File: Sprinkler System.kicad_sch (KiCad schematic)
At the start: 76 parts, among them J1 Main Supply, J2 XFMR_Out, J20 Station_0, J21 Station_1, J22 Station_2, J23 Station_3, J24 Station_4, J25 Station_5, J3 XFMR_In, J4 Conn_Button, J5 UART0, J6 I2C, K1 G3MB-202P, K20 G5LE-1-DC5, K21 G5LE-1-DC5, K22 G5LE-1-DC5, K23 G5LE-1-DC5, K24 G5LE-1-DC5, K25 G5LE-1-DC5, SW1 EN, SW2 BOOT, U1 AMS1117-3.3, U2 EL817, U3 HLK-PM01, U4 ESP32-WROOM-32U, U5 ULN2803A

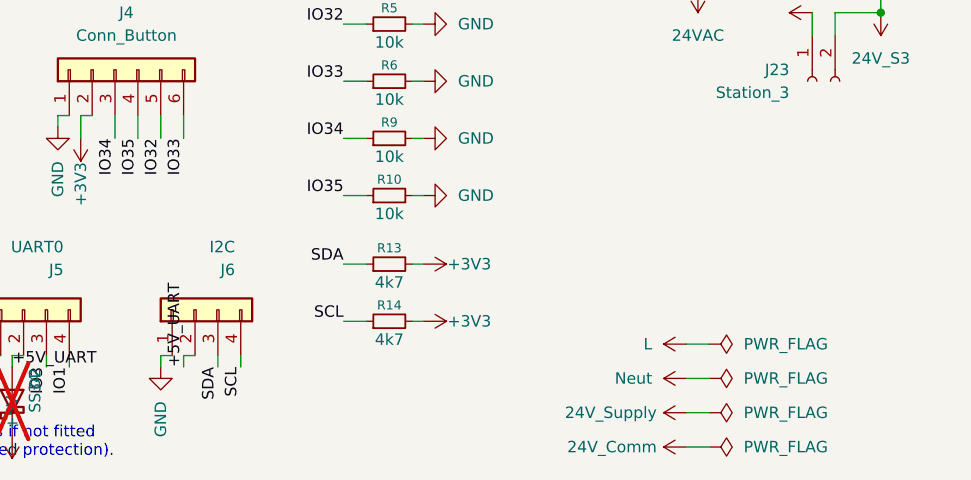
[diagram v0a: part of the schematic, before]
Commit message: Add JP1 solder jumper to select J6 I2C-header supply (3V3 default)
The I2C expansion header J6 previously took the raw +5V_UART branch on
pin 2, which would put 5V on the SDA/SCL pull-ups and any 3V3-logic
peripheral. JP1 (3-way solder jumper on the back) selects J6's VCC:
default-bridged 1-2 = +3V3, re-bridge 2-3 = +5V. J6 pin 2 is now the
/J6_VCC net; J5 pin 2 keeps the true +5V_UART (re-fed from the rail on
F.Cu past the IO-routing on the back), so UART-adapter powering and the
D2 back-feed block are unaffected.

Scope note: the optional TCA9406 level-shifter and SDA/SCL bypass
jumpers from the original plan were dropped - the J5/J6 corner is too
congested to route them cleanly on this revision, and the supply
jumper alone covers the intended use (run a 3V3 I2C device safely, or
switch to 5V if ever needed). Can be revisited interactively later.

Jumper is on B.Cu, silk-labelled. ERC/DRC: 0 violations; zones refilled.

Co-Authored-By: Claude Fable 5 <noreply@anthropic.com>
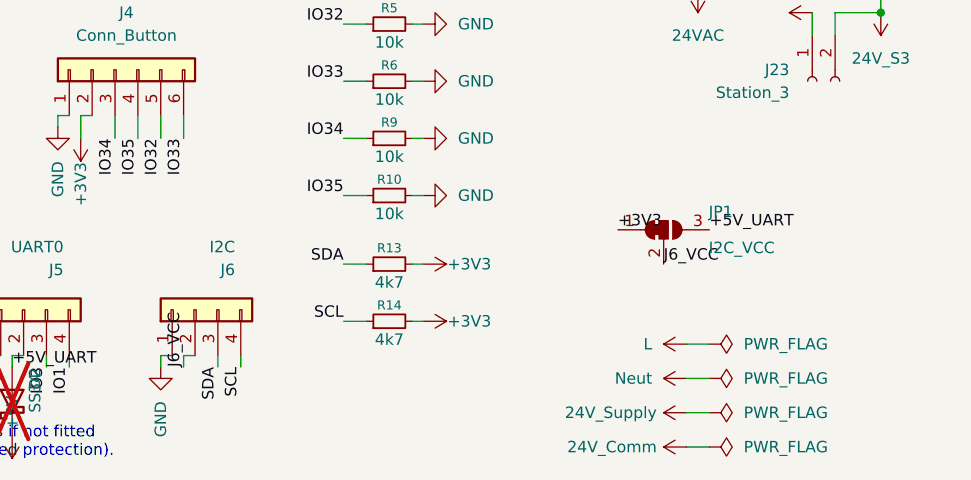
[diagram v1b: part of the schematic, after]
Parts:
- added JP1: I2C_VCC, Jumper:SolderJumper-3_P1.3mm_Bridged12_RoundedPad1.0x1.5mm_NumberLabels, symbol Jumper:SolderJumper_3_Bridged12
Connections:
- net +3V3: now also JP1.1 (A)
- net +5V_UART: now also JP1.3 (B); no longer J6.2 (Pin_2)
- new net J6_VCC: J6.2 (Pin_2), JP1.2 (C)
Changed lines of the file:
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@@
 		)
 	)
-	(label "+5V_UART"
+	(label "J6_VCC"
 		(at 101.6 185.42 90)
 		(effects
@@
 		(effects
 			(font
+				(size 1.27 1.27)
+			)
+			(justify left bottom)
+		)
+	)
+	(symbol
+		(lib_id "Jumper:SolderJumper_3_Bridged12")
+		(at 154.94 170.18 0)
+		(unit 1)
+		(body_style 1)
+		(exclude_from_sim no)
+		(in_bom yes)
+		(on_board yes)
+		(in_pos_files yes)
+		(dnp no)
+		(fields_autoplaced yes)
+		(property "Reference" "JP1"
+			(at 159.94 168.18 0)
+			(show_name no)
+			(do_not_autoplace no)
+			(effects
+				(font
+					(size 1.27 1.27)
+				)
+				(justify left)
+			)
+		)
+		(property "Value" "I2C_VCC"
+			(at 159.94 172.18 0)
+			(show_name no)
+			(do_not_autoplace no)
+			(effects
+				(font
+					(size 1.27 1.27)
+				)
+				(justify left)
+			)
+		)
+		(property "Footprint" "Jumper:SolderJumper-3_P1.3mm_Bridged12_RoundedPad1.0x1.5mm_NumberLabels"
+			(at 154.94 170.18 0)
+			(hide yes)
+			(show_name no)
+			(do_not_autoplace no)
+			(effects
+				(font
+					(size 1.27 1.27)
+				)
+				(justify left)
+			)
+		)
+		(property "Datasheet" ""
+			(at 154.94 170.18 0)
+			(hide yes)
+			(show_name no)
+			(do_not_autoplace no)
+			(effects
+				(font
+					(size 1.27 1.27)
+				)
+				(justify left)
+			)
+		)
+		(property "Description" "J6 supply select: 1-2=3V3 (default bridged), 2-3=5V"
+			(at 154.94 170.18 0)
+			(hide yes)
+			(show_name no)
+			(do_not_autoplace no)
+			(effects
+				(font
+					(size 1.27 1.27)
+				)
+				(justify left)
+			)
+		)
+		(pin "1"
+		)
+		(pin "2"
+		)
+		(pin "3"
+		)
+		(instances
+			(project "Sprinkler System"
+				(path "/8fa12040-b3d8-4f13-b02e-6c4ba5cdd128"
+					(reference "JP1")
+					(unit 1)
+				)
+			)
+		)
+	)
+	(label "+3V3"
+		(at 149.85999999999999 170.18 0)
+		(effects
+			(font
+				(size 1.27 1.27)
+			)
+			(justify left bottom)
+		)
+	)
+	(label "J6_VCC"
+		(at 154.94 173.99 0)
+		(effects
+			(font
+				(size 1.27 1.27)
+			)
+			(justify left bottom)
+		)
+	)
+	(label "+5V_UART"
+		(at 160.02 170.18 0)
+		(effects
+			(font

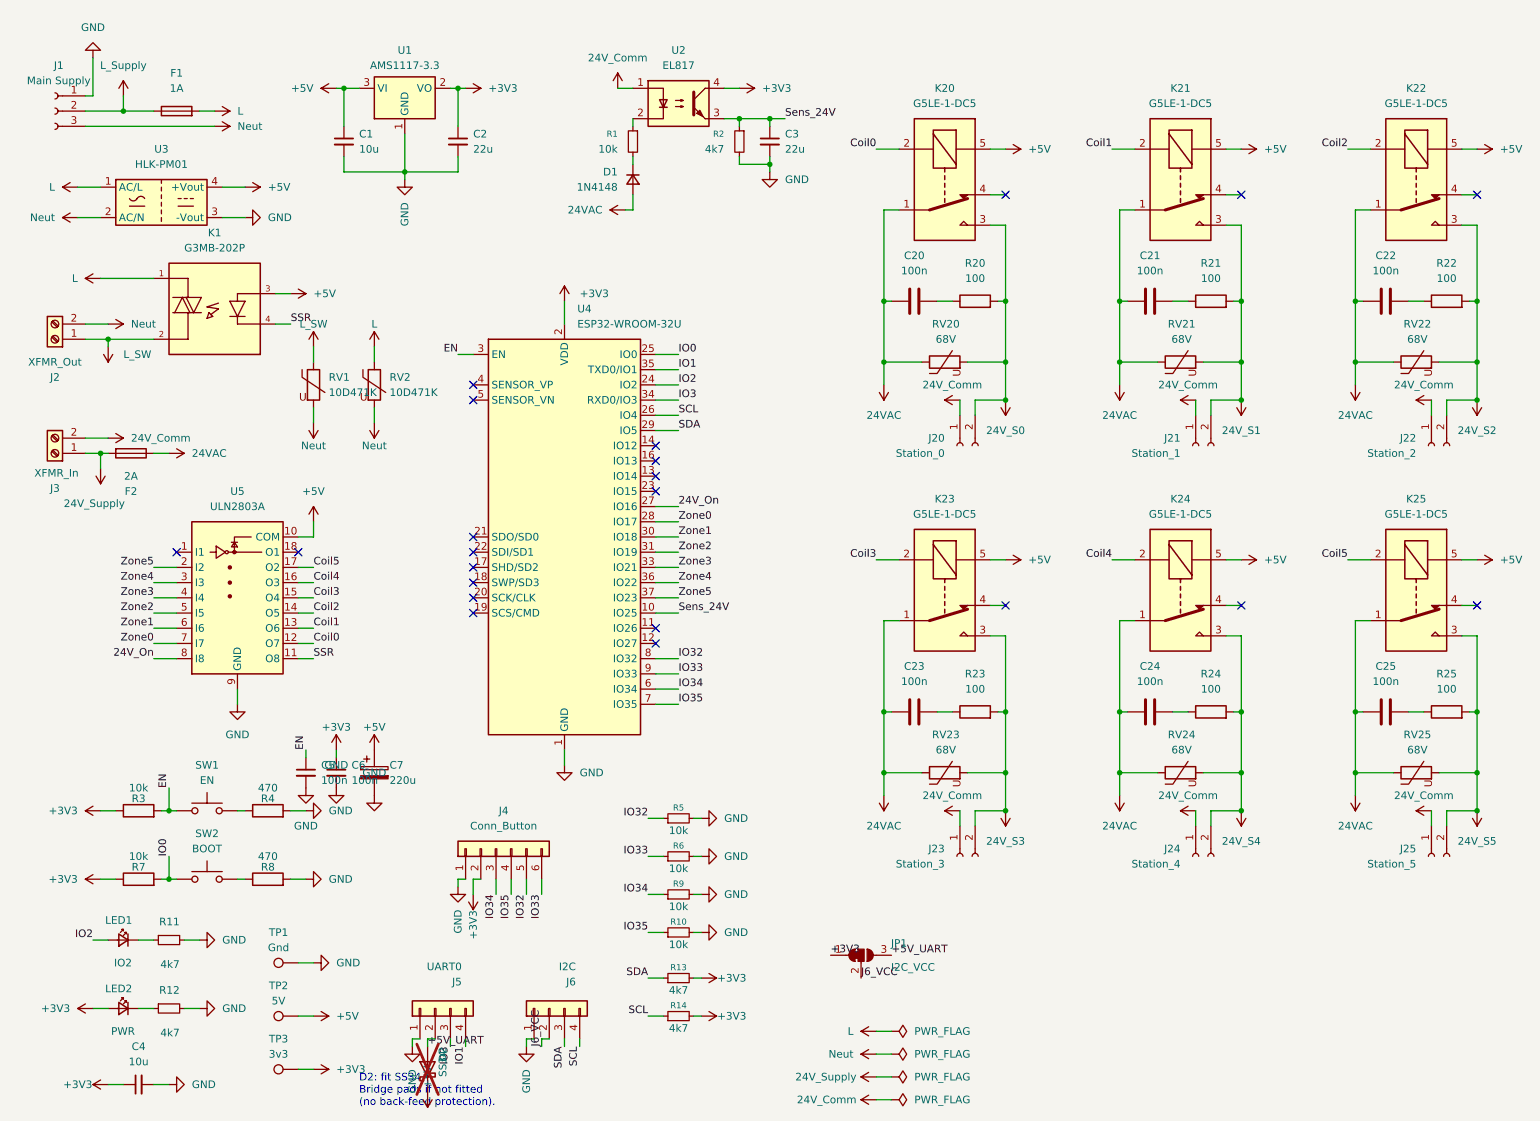
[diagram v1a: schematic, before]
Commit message: Revise board: renumber parts, drop D2, J1 to Phoenix PT 5.0mm
Hand-edited layout changes plus regenerated fabrication outputs:
- Renumber C/R references (EN reset now C6, +5V bulk 220uF now C5,
  ESP32 VDD decoupling C4, +3V3 10uF C7; button pull-downs R5/R8/R10/R11)
- Remove D2 Schottky; J5 pin 2 (UART 5V) now ties directly to +5V
- Replace J1 with Phoenix PT 1,5/3-5.0 (5.0mm, mains-rated) terminal block
- Swap RV1/RV2 roles: RV1 across mains L-N input, RV2 across SSR output
  / transformer primary; RV footprints to stock D12mm_W4mm
- Regenerate gerbers, drill, POS, BOM, netlist, and PDFs to match

Co-Authored-By: Claude Opus 4.8 <noreply@anthropic.com>
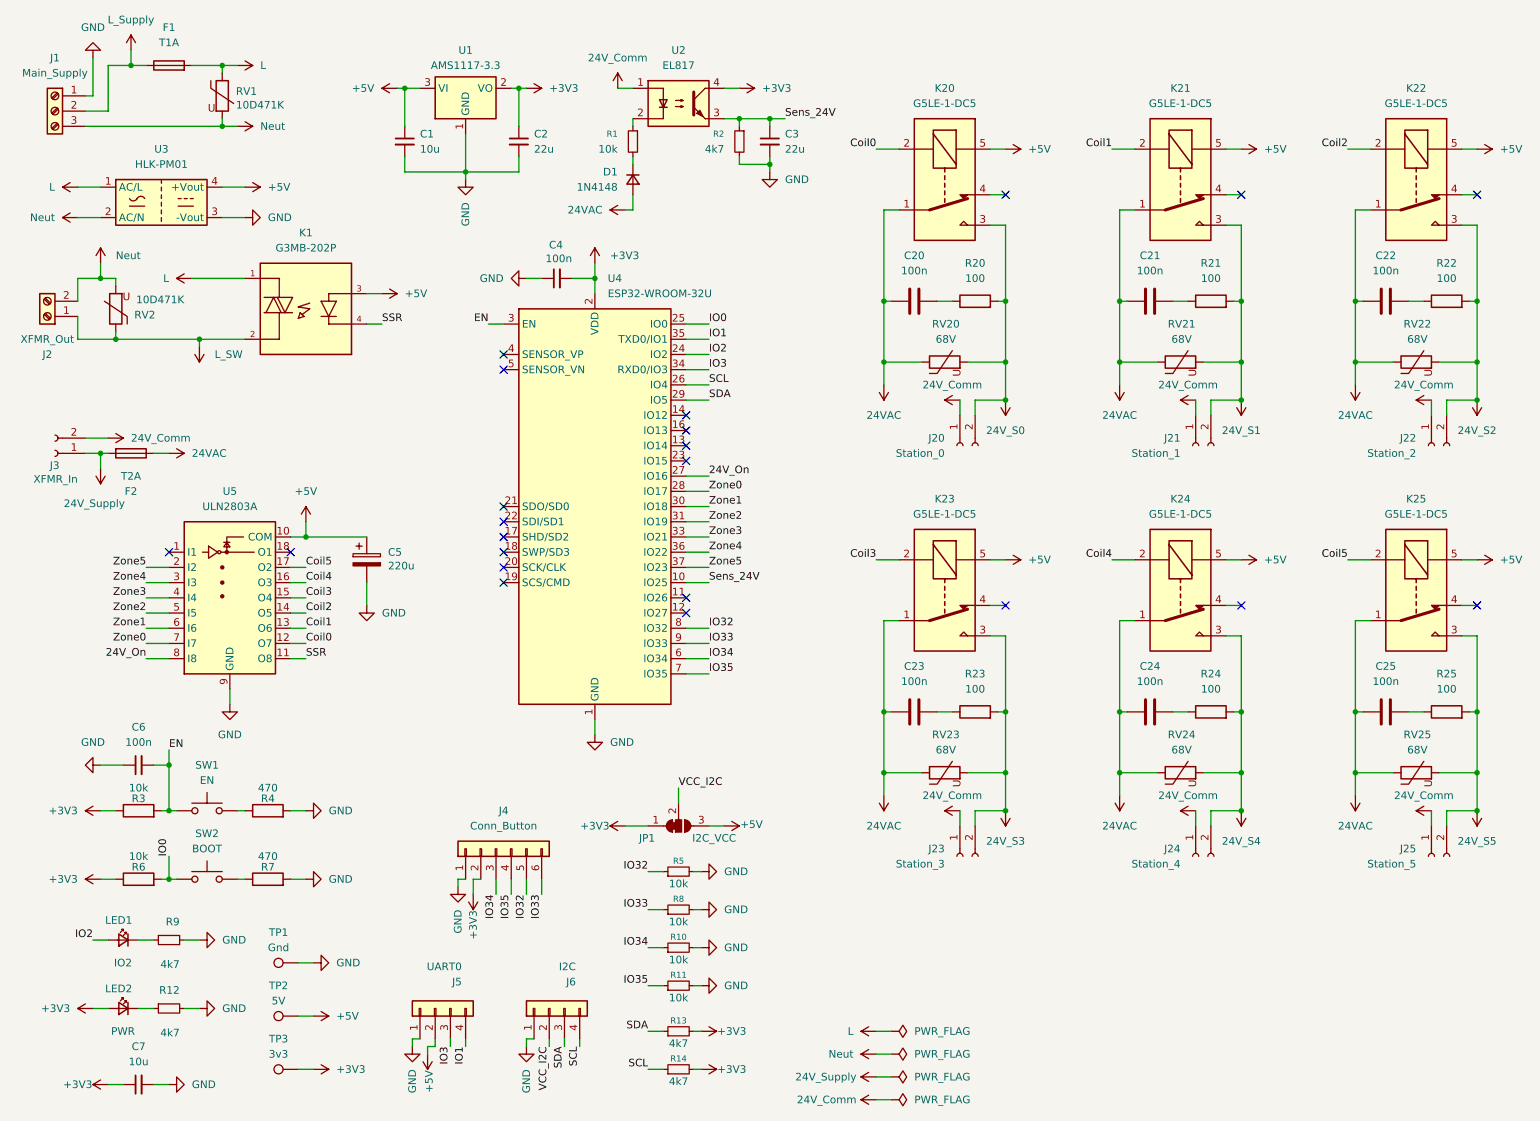
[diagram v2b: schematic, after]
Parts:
- removed D2: SS34, Diode_SMD:D_SMA, symbol Device:D_Schottky
- removed J3: XFMR_In, TerminalBlock_Phoenix:TerminalBlock_Phoenix_PT-1,5-2-5.0-H_1x02_P5.00mm_Horizontal, symbol Connector:Screw_Terminal_01x02
- added J3: XFMR_In, Connector_Phoenix_MC:PhoenixContact_MC_1,5_2-G-3.81_1x02_P3.81mm_Horizontal, symbol Connector:Conn_01x02_Socket
- F1: value 1A -> T1A
- F2: value 2A -> T2A
- J1: value Main Supply -> Main_Supply; footprint Sprinkler System:PhoenixContact_MSTBA_2,5_3-G-5,08_1x03_P5.08mm_Horizontal_EdgeClip -> TerminalBlock_Phoenix:TerminalBlock_Phoenix_PT-1,5-3-5.0-H_1x03_P5.00mm_Horizontal; symbol Connector:Conn_01x03_Socket -> Connector:Screw_Terminal_01x03
- RV1: renamed from RV2; footprint Varistor:RV_Disc_D12mm_W3.9mm_P7.5mm -> Varistor:RV_Disc_D12mm_W4mm_P7.5mm
- RV2: renamed from RV1; footprint Sprinkler System:RV_Disc_D12mm_W3.9mm_P7.5mm_EdgeClip -> Varistor:RV_Disc_D12mm_W4mm_P7.5mm
- renumbered C6 to C4, C7 to C5, C5 to C6, C4 to C7, R9 to R10, R10 to R11, R7 to R6, R8 to R7, R6 to R8, R11 to R9
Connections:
- net +5V_UART is gone; now on net +5V: J5.2 (Pin_2), JP1.3 (B)
- net +3V3: now also C4.2; no longer C4.1
- net 24V_Comm: now also J3.2 (Pin_2)
- net 24V_Supply: now also J3.1 (Pin_1)
- net EN: now also C6.2; no longer C6.1
- net GND: now also C4.1, C6.1; no longer C4.2, C6.2
- net J6_VCC renamed VCC_I2C
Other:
- note removed: "D2: fit SS34. Bridge pads if not fitted (no back-feed protection)."
- moved on the sheet: C1, C2, C4, C5, C6, F1, J2, JP1, K1, R10, R11, R13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

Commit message: Add title block to schematic and PCB
Co-Authored-By: Claude Sonnet 4.6 <noreply@anthropic.com>
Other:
- title: (none) -> ESPHome Sprinkler System
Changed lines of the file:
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@@
 	(generator_version "10.0")
 	(paper "A4")
+	(title_block
+		(title "ESPHome Sprinkler System")
+		(date "2026-06-26")
+		(rev "v1.0.0-1-gb064c0c")
+	)
 	(junction
 		(at 39.37 146.05)
